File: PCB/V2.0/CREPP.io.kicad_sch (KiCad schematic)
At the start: 7 parts, among them J19 Analog_Inputs

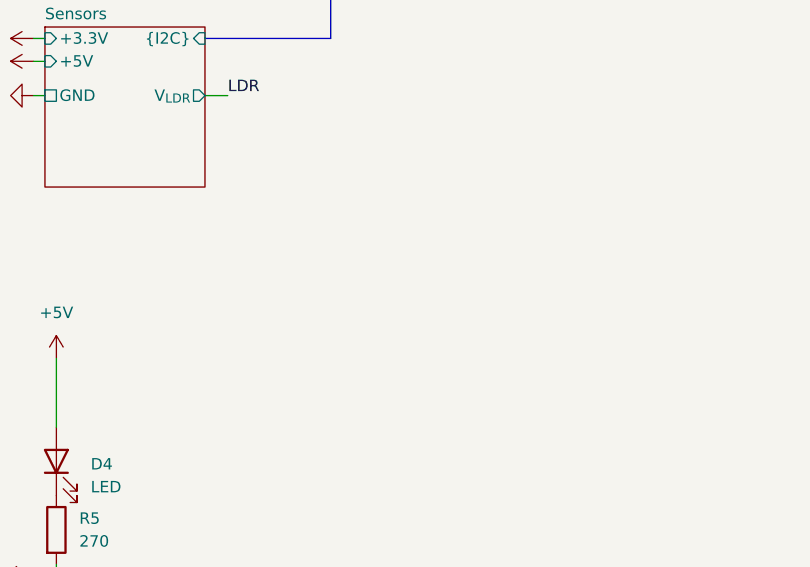
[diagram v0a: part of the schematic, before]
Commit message: Update 2.0 - IMU and NRF24 support
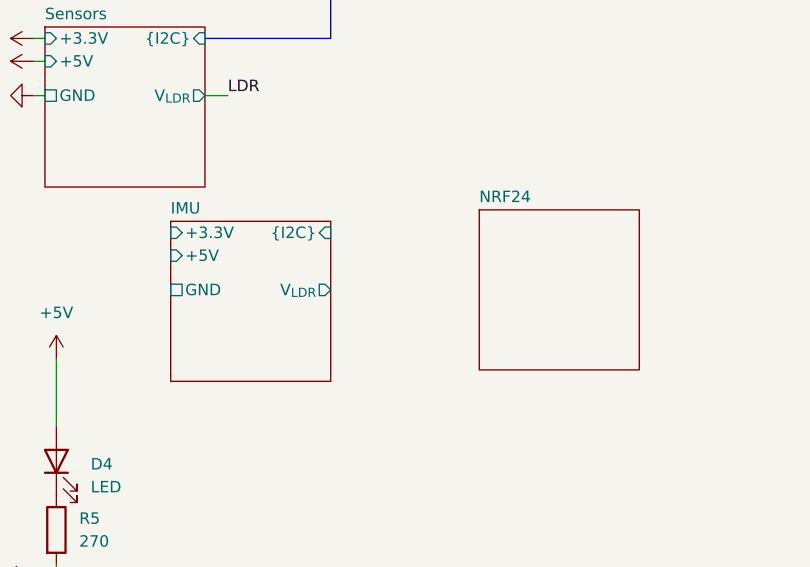
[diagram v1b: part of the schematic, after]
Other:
- added sheet IMU (Modules/IMU.kicad_sch)
- added sheet NRF24 (Modules/NRF24.kicad_sch)
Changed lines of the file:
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@@
+	)
+	(sheet
+		(at 86.36 127)
+		(size 17.78 17.78)
+		(fields_autoplaced yes)
+		(stroke
+			(width 0.1524)
+			(type solid)
+		)
+		(fill
+			(color 0 0 0 0.0000)
+		)
+		(property "Sheetname" "NRF24"
+			(at 86.36 126.2884 0)
+			(effects
+				(font
+					(size 1.27 1.27)
+				)
+				(justify left bottom)
+			)
+		)
+		(property "Sheetfile" "Modules/NRF24.kicad_sch"
+			(at 86.36 145.3646 0)
+			(effects
+				(font
+					(size 1.27 1.27)
+				)
+				(justify left top)
+				(hide yes)
+			)
+		)
+		(instances
+			(project "CREPP.io"
+				(path "/8bcd0d00-b75f-4070-8d50-196a2022a31c"
+					(page "12")
+				)
+			)
+		)
 	)
 	(sheet
@@
 				)
 			)
+		)
+	)
+	(sheet
+		(at 52.07 128.27)
+		(size 17.78 17.78)
+		(fields_autoplaced yes)
+		(stroke
+			(width 0.1524)
+			(type solid)
+		)
+		(fill
+			(color 0 0 0 0.0000)
+		)
+		(property "Sheetname" "IMU"
+			(at 52.07 127.5584 0)
+			(effects
+				(font
+					(size 1.27 1.27)
+				)
+				(justify left bottom)
+			)
+		)
+		(property "Sheetfile" "Modules/IMU.kicad_sch"
+			(at 52.07 146.6346 0)
+			(effects
+				(font
+					(size 1.27 1.27)
+				)
+				(justify left top)
+				(hide yes)
+			)
+		)
+		(pin "GND" passive
+			(at 52.07 135.89 180)
+			(effects
+				(font
+					(size 1.27 1.27)
+				)
+				(justify left)
+			)
+		)
+		(pin "+3.3V" input
+			(at 52.07 129.54 180)
+			(effects
+				(font
+					(size 1.27 1.27)
+				)
+				(justify left)
+			)
+		)
+		(pin "V_{LDR}" output
+			(at 69.85 135.89 0)
+			(effects
+				(font
+					(size 1.27 1.27)
+				)
+				(justify right)
+			)
+		)
+		(pin "+5V" input
+			(at 52.07 132.08 180)
+			(effects
+				(font
+					(size 1.27 1.27)
+				)
+				(justify left)
+			)
+		)
+		(pin "{I2C}" input
+			(at 69.85 129.54 0)
+			(effects
+				(font
+					(size 1.27 1.27)
+				)
+				(justify right)
+			)
+		)
+		(instances
+			(project "CREPP.io"
+				(path "/8bcd0d00-b75f-4070-8d50-196a2022a31c"
+					(page "10")
+				)
+			)

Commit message: Add RTC
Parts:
- removed J19: Analog_Inputs, Connector_PinHeader_2.54mm:PinHeader_1x04_P2.54mm_Vertical, symbol Connector:Conn_01x04_Socket
- R5: footprint Resistor_THT:R_Axial_DIN0207_L6.3mm_D2.5mm_P7.62mm_Horizontal -> Resistor_THT:R_Axial_DIN0207_L6.3mm_D2.5mm_P10.16mm_Horizontal
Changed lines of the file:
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@@
-	(wire
-		(pts
-			(xy 29.21 87.63) (xy 38.1 87.63)
-		)
-		(stroke
-			(width 0)
-			(type default)
-		)
-	)
 	(wire
 		(pts
@@
 	(wire
 		(pts
-			(xy 29.21 90.17) (xy 38.1 90.17)
-		)
-		(stroke
-			(width 0)
-			(type default)
-		)
-	)
-	(wire
-		(pts
 			(xy 161.29 78.74) (xy 162.56 78.74)
 		)
@@
 		)
 	)
-	(wire
-		(pts
-			(xy 29.21 95.25) (xy 38.1 95.25)
-		)
-		(stroke
-			(width 0)
-			(type default)
-		)
-	)
 	(bus
 		(pts
@@
 		(pts
 			(xy 106.68 88.9) (xy 106.68 91.44)
-		)
-		(stroke
-			(width 0)
-			(type default)
-		)
-	)
-	(wire
-		(pts
-			(xy 29.21 92.71) (xy 38.1 92.71)
 		)
 		(stroke
@@
 		)
 	)
-	(label "LDR"
-		(at 35.56 87.63 180)
-		(fields_autoplaced yes)
-		(effects
-			(font
-				(size 1.27 1.27)
-			)
-			(justify right bottom)
-		)
-	)
 	(symbol
 		(lib_id "Device:R")
@@
 			)
 		)
-		(property "Footprint" "Resistor_THT:R_Axial_DIN0207_L6.3mm_D2.5mm_P7.62mm_Horizontal"
+		(property "Footprint" "Resistor_THT:R_Axial_DIN0207_L6.3mm_D2.5mm_P10.16mm_Horizontal"
 			(at 37.592 162.56 90)
 			(effects
@@
 					(unit 1)
 				)
-			)
-		)
-	)
-	(symbol
-		(lib_id "Connector:Conn_01x04_Socket")
-		(at 24.13 92.71 180)
-		(unit 1)
-		(exclude_from_sim no)
-		(in_bom yes)
-		(on_board yes)
-		(dnp no)
-		(fields_autoplaced yes)
-		(property "Reference" "J19"
-			(at 24.765 82.55 0)
-			(effects
-				(font
-					(size 1.27 1.27)
-				)
-			)
-		)
-		(property "Value" "Analog_Inputs"
-			(at 24.765 85.09 0)
-			(effects
-				(font
-					(size 1.27 1.27)
-				)
-			)
-		)
-		(property "Footprint" "Connector_PinHeader_2.54mm:PinHeader_1x04_P2.54mm_Vertical"
-			(at 24.13 92.71 0)
-			(effects
-				(font
-					(size 1.27 1.27)
-				)
-				(hide yes)
-			)
-		)
-		(property "Datasheet" "~"
-			(at 24.13 92.71 0)
-			(effects
-				(font
-					(size 1.27 1.27)
-				)
-				(hide yes)
-			)
-		)
-		(property "Description" "Generic connector, single row, 01x04, script generated"
-			(at 24.13 92.71 0)
-			(effects
-				(font
-					(size 1.27 1.27)
-				)
-				(hide yes)
-			)
-		)
-		(pin "4"
-		)
-		(pin "3"
-		)
-		(pin "2"
-		)
-		(pin "1"
-		)
-		(instances
-			(project "CREPP.io"
-				(path "/8bcd0d00-b75f-4070-8d50-196a2022a31c"
-					(reference "J19")
-					(unit 1)
-				)

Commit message: Add codes
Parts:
- added J19, J20, J21: Conn_01x04_Socket, Connector_JST:JST_PH_B4B-PH-K_1x04_P2.00mm_Vertical, symbol Connector:Conn_01x04_Socket
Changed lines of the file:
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@@
+	)
+	(symbol
+		(lib_id "Connector:Conn_01x04_Socket")
+		(at 232.41 81.28 0)
+		(unit 1)
+		(exclude_from_sim no)
+		(in_bom yes)
+		(on_board yes)
+		(dnp no)
+		(fields_autoplaced yes)
+		(property "Reference" "J20"
+			(at 233.68 81.2799 0)
+			(effects
+				(font
+					(size 1.27 1.27)
+				)
+				(justify left)
+			)
+		)
+		(property "Value" "Conn_01x04_Socket"
+			(at 233.68 83.8199 0)
+			(effects
+				(font
+					(size 1.27 1.27)
+				)
+				(justify left)
+			)
+		)
+		(property "Footprint" "Connector_JST:JST_PH_B4B-PH-K_1x04_P2.00mm_Vertical"
+			(at 232.41 81.28 0)
+			(effects
+				(font
+					(size 1.27 1.27)
+				)
+				(hide yes)
+			)
+		)
+		(property "Datasheet" "~"
+			(at 232.41 81.28 0)
+			(effects
+				(font
+					(size 1.27 1.27)
+				)
+				(hide yes)
+			)
+		)
+		(property "Description" "Generic connector, single row, 01x04, script generated"
+			(at 232.41 81.28 0)
+			(effects
+				(font
+					(size 1.27 1.27)
+				)
+				(hide yes)
+			)
+		)
+		(pin "1"
+		)
+		(pin "4"
+		)
+		(pin "3"
+		)
+		(pin "2"
+		)
+		(instances
+			(project "CREPP.io"
+				(path "/8bcd0d00-b75f-4070-8d50-196a2022a31c"
+					(reference "J20")
+					(unit 1)
+				)
+			)
+		)
+	)
+	(symbol
+		(lib_id "Connector:Conn_01x04_Socket")
+		(at 232.41 69.85 0)
+		(unit 1)
+		(exclude_from_sim no)
+		(in_bom yes)
+		(on_board yes)
+		(dnp no)
+		(fields_autoplaced yes)
+		(property "Reference" "J19"
+			(at 233.68 69.8499 0)
+			(effects
+				(font
+					(size 1.27 1.27)
+				)
+				(justify left)
+			)
+		)
+		(property "Value" "Conn_01x04_Socket"
+			(at 233.68 72.3899 0)
+			(effects
+				(font
+					(size 1.27 1.27)
+				)
+				(justify left)
+			)
+		)
+		(property "Footprint" "Connector_JST:JST_PH_B4B-PH-K_1x04_P2.00mm_Vertical"
+			(at 232.41 69.85 0)
+			(effects
+				(font
+					(size 1.27 1.27)
+				)
+				(hide yes)
+			)
+		)
+		(property "Datasheet" "~"
+			(at 232.41 69.85 0)
+			(effects
+				(font
+					(size 1.27 1.27)
+				)
+				(hide yes)
+			)
+		)
+		(property "Description" "Generic connector, single row, 01x04, script generated"
+			(at 232.41 69.85 0)
+			(effects
+				(font
+					(size 1.27 1.27)
+				)
+				(hide yes)
+			)
+		)
+		(pin "1"
+		)
+		(pin "4"
+		)
+		(pin "3"
+		)
+		(pin "2"
+		)
+		(instances
+			(project "CREPP.io"
+				(path "/8bcd0d00-b75f-4070-8d50-196a2022a31c"
+					(reference "J19")
+					(unit 1)
+				)
+			)
+		)
 	)
 	(symbol
@@
 					(unit 1)
 				)
+			)
+		)
+	)
+	(symbol
+		(lib_id "Connector:Conn_01x04_Socket")
+		(at 232.41 59.69 0)
+		(unit 1)
+		(exclude_from_sim no)
+		(in_bom yes)
+		(on_board yes)
+		(dnp no)
+		(fields_autoplaced yes)
+		(property "Reference" "J21"
+			(at 233.68 59.6899 0)
+			(effects
+				(font
+					(size 1.27 1.27)
+				)
+				(justify left)
+			)
+		)
+		(property "Value" "Conn_01x04_Socket"
+			(at 233.68 62.2299 0)
+			(effects
+				(font
+					(size 1.27 1.27)
+				)
+				(justify left)
+			)
+		)
+		(property "Footprint" "Connector_JST:JST_PH_B4B-PH-K_1x04_P2.00mm_Vertical"
+			(at 232.41 59.69 0)
+			(effects
+				(font
+					(size 1.27 1.27)
+				)
+				(hide yes)
+			)
+		)
+		(property "Datasheet" "~"
+			(at 232.41 59.69 0)
+			(effects
+				(font
+					(size 1.27 1.27)
+				)
+				(hide yes)
+			)
+		)
+		(property "Description" "Generic connector, single row, 01x04, script generated"
+			(at 232.41 59.69 0)
+			(effects
+				(font
+					(size 1.27 1.27)
+				)
+				(hide yes)
+			)
+		)
+		(pin "1"
+		)
+		(pin "4"
+		)
+		(pin "3"
+		)
+		(pin "2"
+		)
+		(instances
+			(project "CREPP.io"
+				(path "/8bcd0d00-b75f-4070-8d50-196a2022a31c"
+					(reference "J21")
+					(unit 1)
+				)

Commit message: Update V2.0 form factor
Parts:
- removed J19, J21: Conn_01x04_Socket, Connector_JST:JST_PH_B4B-PH-K_1x04_P2.00mm_Vertical, symbol Connector:Conn_01x04_Socket
- added J31: ST_PH_B4B-PH-K_1x04_P2.00mm, Connector_JST:JST_PH_B4B-PH-K_1x04_P2.00mm_Vertical, symbol Connector:Conn_01x04_Socket
- J20: value Conn_01x04_Socket -> ST_PH_B4B-PH-K_1x04_P2.00mm
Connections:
- no-connect marks 8 -> 2
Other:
- removed sheet IO_Extender
- added sheet I2C_Interface (Modules/I2C_Interface.kicad_sch)
- added sheet MOSFET (Modules/MOSFET.kicad_sch)
- added sheet Motors (Modules/Motors.kicad_sch)
- sheet MCU ports: added GP0, GP1, GP10, GP11, GP12, GP13, GP14, GP15, GP2, GP3, GP4, GP5, GP6, GP7, GP8, GP9; removed +3.3V, +5V, ADC, CS, EN, GPIO0_D3, GPIO12_D6, GPIO13_D7_RX2, GPIO14_D5, GPIO15_D8_TX2, GPIO16_D0, GPIO1_TX, GPIO2_D4_INTERNAL_LED, GPIO3_RX, GPIO4_D2_SDA, GPIO5_D1_SCL, RESET, {I2C}, {SPI}, {UART}
- sheet NRF24 ports: added +3.3V, CE, GND, MISO, MOSI, SCK, ~{CSN}; removed none
- sheet RTC ports: added {SPI}; removed {I2C}
- moved on the sheet: D4, H1, H2, H3, H4, J20, R5

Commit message: Add img
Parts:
- added S1, S2, S3, S4: ~, CREPP_Spacers:Spacer_M3_FF_20mm, symbol CREPP_Spacers:Spacer_M3_Parametric

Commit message: Update board
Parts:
- removed J20, J31: ST_PH_B4B-PH-K_1x04_P2.00mm, Connector_JST:JST_PH_B4B-PH-K_1x04_P2.00mm_Vertical, symbol Connector:Conn_01x04_Socket
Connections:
- no-connect marks 2 -> 1
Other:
- sheet Power renamed Servo_Power
- sheet I2C_Interface ports: added {I2C0}; removed +5V, {I2C}
- sheet IMU ports: added {I2C0}; removed +5V, V_{LDR}, {I2C}
- sheet MCU ports: added +3.3V, GP16, GP17, GP18, GP19, GP20, GP21, GP22, GP26, GP27, GP28, RUN, V_{BUS}, V_{SYS}, {I2C0}; removed GP4, GP5
- sheet OLED ports: added {I2C0}; removed {I2C}
- sheet RTC ports: added {I2C0}; removed {SPI}
- sheet Sensors ports: added {I2C0}; removed {I2C}
- sheet Servo_Power: file Modules/Power.kicad_sch -> Modules/Servo_Power.kicad_sch
- sheet UserActions ports: added CLK, DT, PB_CENTER; removed none
- moved on the sheet: D4, H1, H2, H3, H4, R5, S1, S2, S3, S4

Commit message: Update
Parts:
- removed D4: LED, LED_THT:LED_D5.0mm, symbol Device:LED
- removed R5: 270, Resistor_THT:R_Axial_DIN0207_L6.3mm_D2.5mm_P10.16mm_Horizontal, symbol Device:R
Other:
- added sheet HC-SR04 (Modules/HC-SR04.kicad_sch)
- added sheet IO_Extender (Modules/IO_Extender.kicad_sch)
- added sheet Power_Supply (Modules/Power_Supplykicad_sch.kicad_sch)
- added sheet Power_Supply1 (Modules/Power_Supplykicad_sch.kicad_sch)
- sheet LED ports: added +5V, DEFAULT_LED, L1, L2, L3, L4, L5; removed GREEN, ORANGE_LED, RED_LED
- moved on the sheet: H1, H2, H3, H4, S2, S3, S4
